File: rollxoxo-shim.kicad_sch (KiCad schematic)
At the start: 1 part, among them J1 Conn_01x10

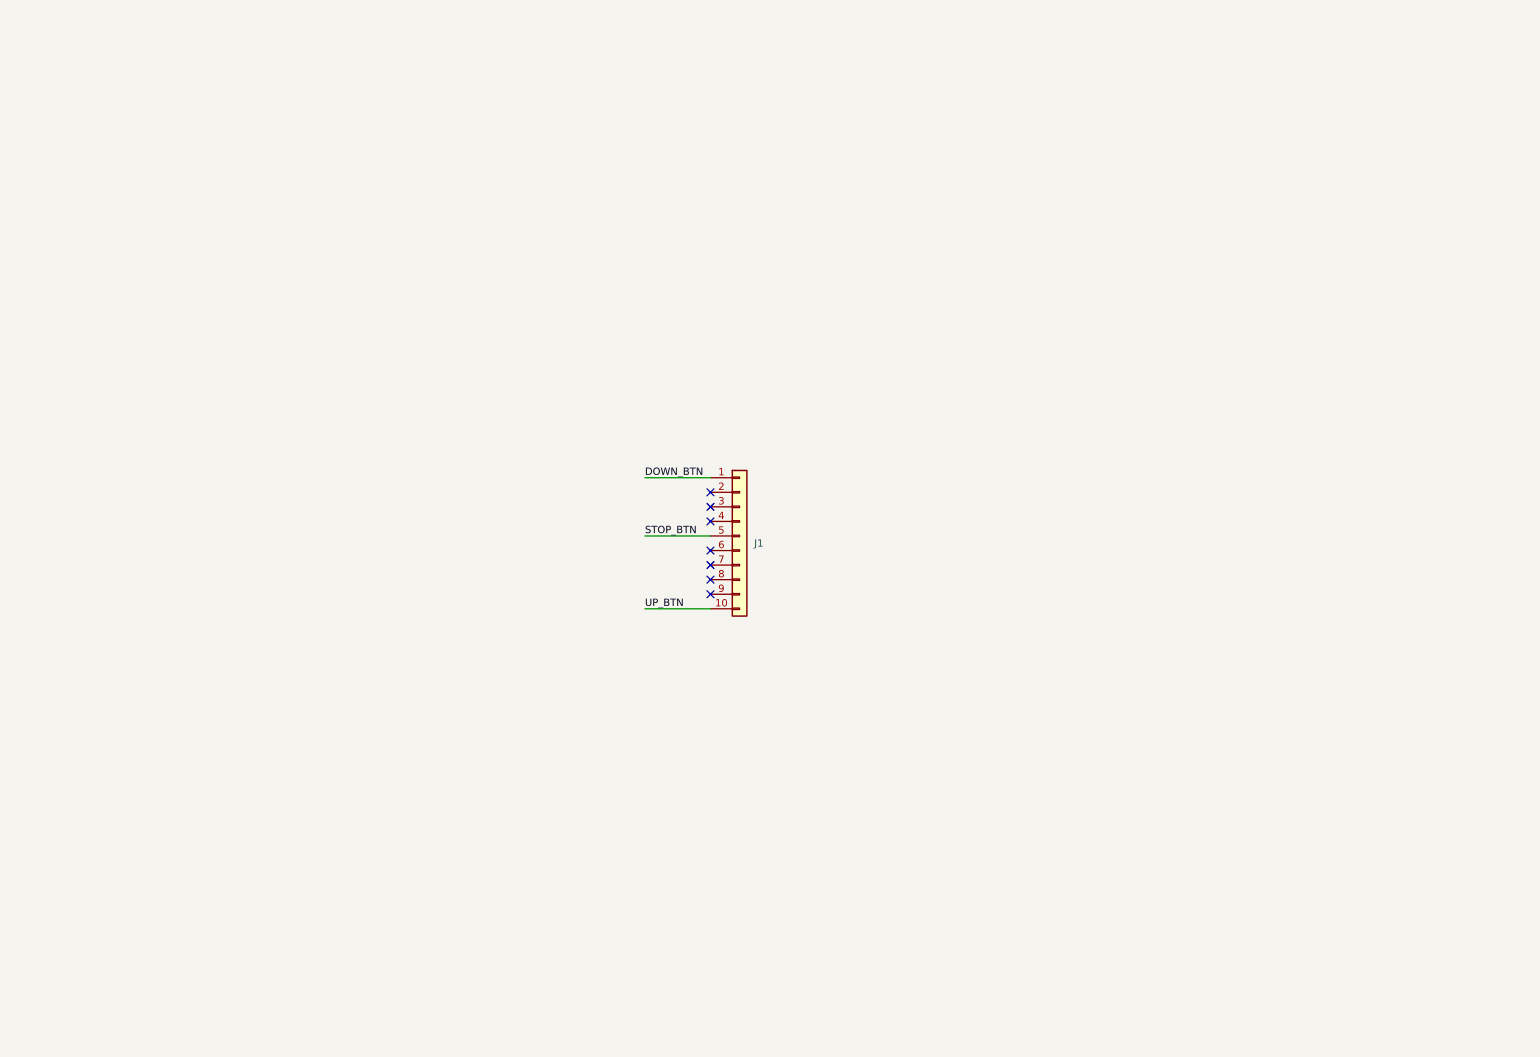
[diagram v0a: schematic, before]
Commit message: schem: import esp32 and support circuits
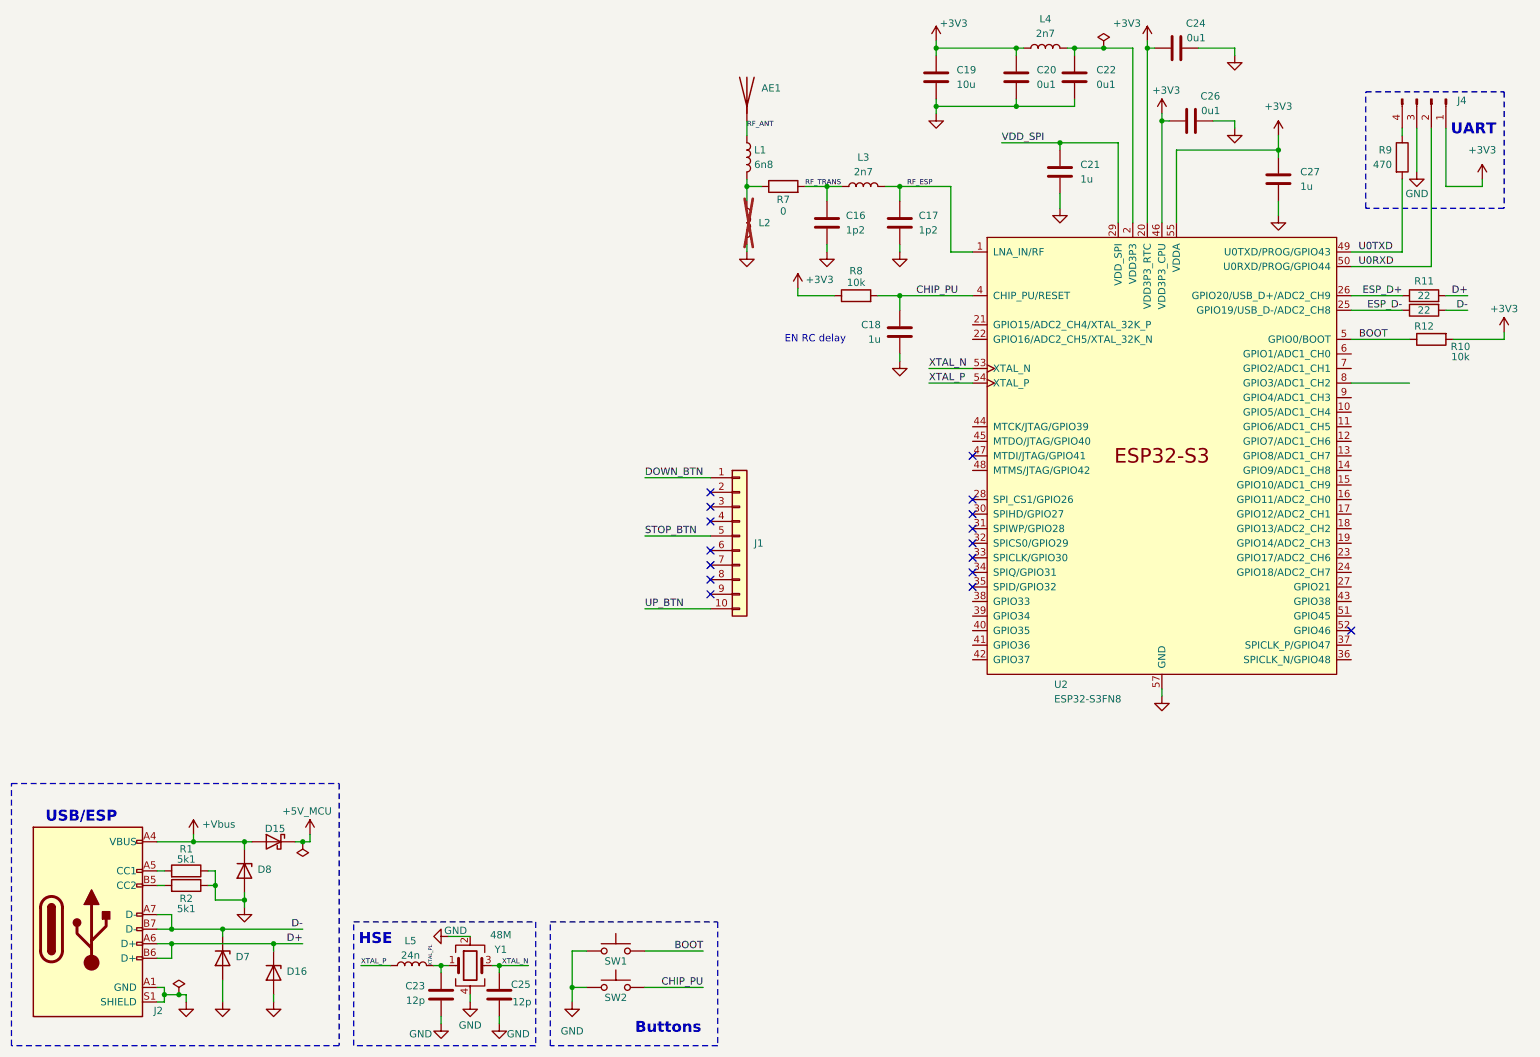
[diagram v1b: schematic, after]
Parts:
- added AE1: Antenna, RF_Antenna:Johanson_2450AT18x100, symbol Device:Antenna
- added C16, C17: 1p2, Capacitor_SMD:C_0402_1005Metric, symbol Device:C
- added C18, C21, C27: 1u, Capacitor_SMD:C_0402_1005Metric, symbol Device:C
- added C19: 10u, Capacitor_SMD:C_0402_1005Metric, symbol Device:C
- added C20, C22, C24, C26: 0u1, Capacitor_SMD:C_0402_1005Metric, symbol Device:C
- added C23, C25: 12p, Capacitor_SMD:C_0402_1005Metric, symbol Device:C
- added D15: D_Schottky, Diode_SMD:D_SMA, symbol Device:D_Schottky
- added D16, D7, D8: H5VU10U, GLCS:Diode_DFN1006, symbol GLCS:H5VU10U
- added J2: USB_C_Receptacle_USB2.0_14P, Connector_USB:USB_C_Receptacle_HRO_TYPE-C-31-M-12, symbol Connector:USB_C_Receptacle_USB2.0_14P
- added J4: Conn_01x04_Pin, Connector_PinHeader_2.54mm:PinHeader_1x04_P2.54mm_Vertical, symbol Connector:Conn_01x04_Pin
- added L1: 6n8, Inductor_SMD:L_0402_1005Metric, symbol Device:L
- added L2: L, Inductor_SMD:L_0402_1005Metric, symbol Device:L
- added L3, L4: 2n7, Inductor_SMD:L_0402_1005Metric, symbol Device:L
- added L5: 24n, Inductor_SMD:L_0402_1005Metric, symbol Device:L
- added R1, R2: 5k1, Resistor_SMD:R_0402_1005Metric, symbol Device:R
- added R10, R8: 10k, Resistor_SMD:R_0402_1005Metric, symbol Device:R
- added R11, R12: 22, Resistor_SMD:R_0402_1005Metric, symbol Device:R
- added R7: 0, Resistor_SMD:R_0402_1005Metric, symbol Device:R
- added R9: 470, Resistor_SMD:R_0402_1005Metric, symbol Device:R
- added SW1, SW2: SW_Push, Button_Switch_SMD:SW_SPST_TS-1088-xR020, symbol Switch:SW_Push
- added U2: ESP32-S3FN8, Package_DFN_QFN:QFN-56-1EP_7x7mm_P0.4mm_EP4x4mm_ThermalVias, symbol PCM_Espressif:ESP32-S3
- added Y1: 48M, Crystal:Crystal_SMD_2016-4Pin_2.0x1.6mm, symbol Device:Crystal_GND24
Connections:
- new net: J2.B5 (CC2), R2.2
- new net: L1.2, L2.1, R7.1
- new net: J4.4 (Pin_4), R9.1
- new net: J2.A5 (CC1), R1.2
- new net +3V3: C19.1, C20.1, C24.1, C26.1, C27.1, J4.1 (Pin_1), L4.1, R10.2, R8.1, U2.20 (VDD3P3_RTC), U2.46 (VDD3P3_CPU), U2.55 (VDDA), U2.56 (VDDA)
- new net +5V_MCU: D15.1 (K)
- new net +Vbus: D15.2 (A), D8.1 (K), J2.A4 (VBUS), J2.A9 (VBUS), J2.B4 (VBUS), J2.B9 (VBUS)
- new net BOOT: R10.1, SW1.2, U2.5 (GPIO0/BOOT)
- new net CHIP_PU: C18.1, R8.2, SW2.2, U2.4 (CHIP_PU/RESET)
- new net D+: D16.1 (K), J2.A6 (D+), J2.B6 (D+), R11.2
- new net D-: D7.1 (K), J2.A7 (D-), J2.B7 (D-), R12.2
- new net ESP_D+: R11.1, U2.26 (GPIO20/USB_D+/ADC2_CH9)
- new net ESP_D-: R12.1, U2.25 (GPIO19/USB_D-/ADC2_CH8)
- new net GND: C16.2, C17.2, C18.2, C19.2, C20.2, C21.2, C22.2, C23.1, C24.2, C25.2, C26.2, C27.2, D16.2 (A), D7.2 (A), D8.2 (A), J2.A1 (GND), J2.A12 (GND), J2.B1 (GND), J2.B12 (GND), J2.S1 (SHIELD), J4.3 (Pin_3), L2.2, R1.1, R2.1, SW1.1, SW2.1, U2.57 (GND), Y1.2, Y1.4
- new net RF_ANT: AE1.1 (A), L1.1
- new net RF_ESP: C17.1, L3.2, U2.1 (LNA_IN/RF)
- new net RF_TRANS: C16.1, L3.1, R7.2
- new net U0RXD: J4.2 (Pin_2), U2.50 (U0RXD/PROG/GPIO44)
- new net U0TXD: R9.2, U2.49 (U0TXD/PROG/GPIO43)
- new net VDD3P3: C22.1, L4.2, U2.2 (VDD3P3), U2.3 (VDD3P3)
- new net VDD_SPI: C21.1, U2.29 (VDD_SPI)
- new net XTAL_N: C25.1, U2.53 (XTAL_N), Y1.3
- new net XTAL_P: L5.1, U2.54 (XTAL_P)
- new net XTAL_PL: C23.2, L5.2, Y1.1
- no-connect marks 7 -> 16
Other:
- note added: "Buttons"
- note added: "EN RC delay"
- note added: "HSE"
- note added: "UART"
- note added: "USB/ESP"

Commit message: schem: add SN74LV1T125DBV level shifters
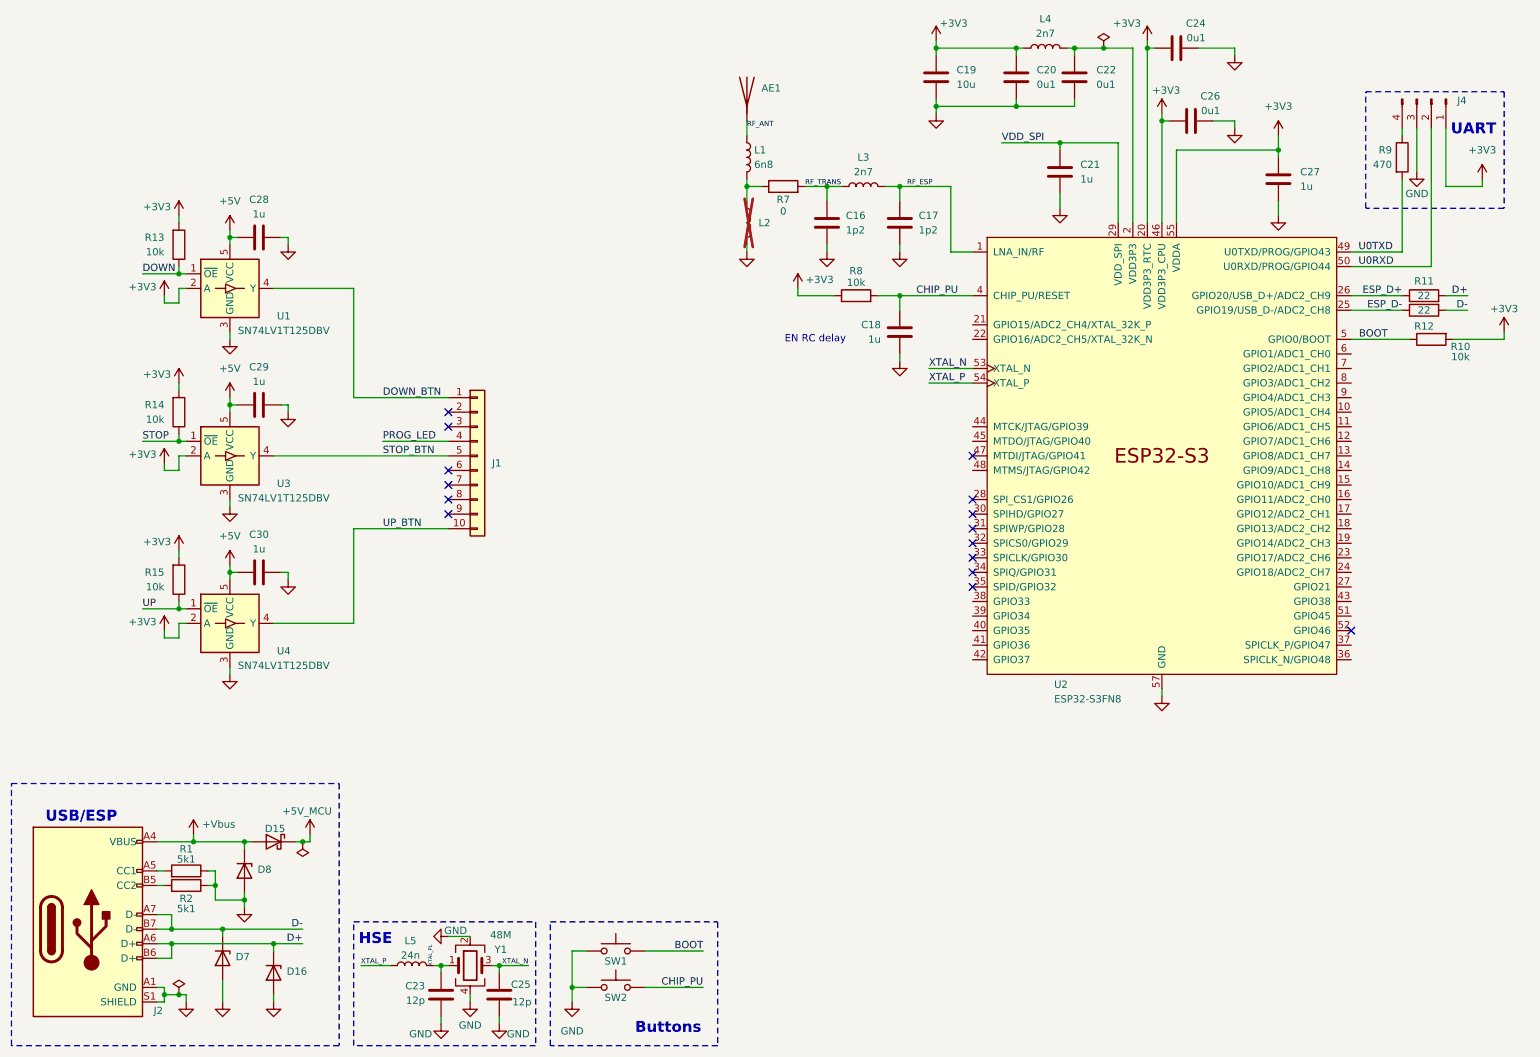
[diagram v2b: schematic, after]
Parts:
- added C28, C29, C30: 1u, Capacitor_SMD:C_0402_1005Metric, symbol Device:C
- added R13, R14, R15: 10k, Resistor_SMD:R_0402_1005Metric, symbol Device:R
- added U1, U3, U4: SN74LV1T125DBV, Package_TO_SOT_SMD:SOT-23-5, symbol Logic_LevelTranslator:SN74LV1T125DBV
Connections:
- net +3V3: now also R13.2, R14.2, R15.2, U1.2 (A), U3.2 (A), U4.2 (A)
- net DOWN_BTN: now also U1.4 (Y)
- net GND: now also C28.2, C29.2, C30.2, U1.3 (GND), U3.3 (GND), U4.3 (GND)
- net STOP_BTN: now also U3.4 (Y)
- net UP_BTN: now also U4.4 (Y)
- net PROG_LED: now reaches J1.4 (Pin_4)
- new net +5V: C28.1, C29.1, C30.1, U1.5 (VCC), U3.5 (VCC), U4.5 (VCC)
- new net DOWN: R13.1, U1.1 (~{OE})
- new net STOP: R14.1, U3.1 (~{OE})
- new net UP: R15.1, U4.1 (~{OE})
- no-connect marks 16 -> 15
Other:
- moved on the sheet: J1

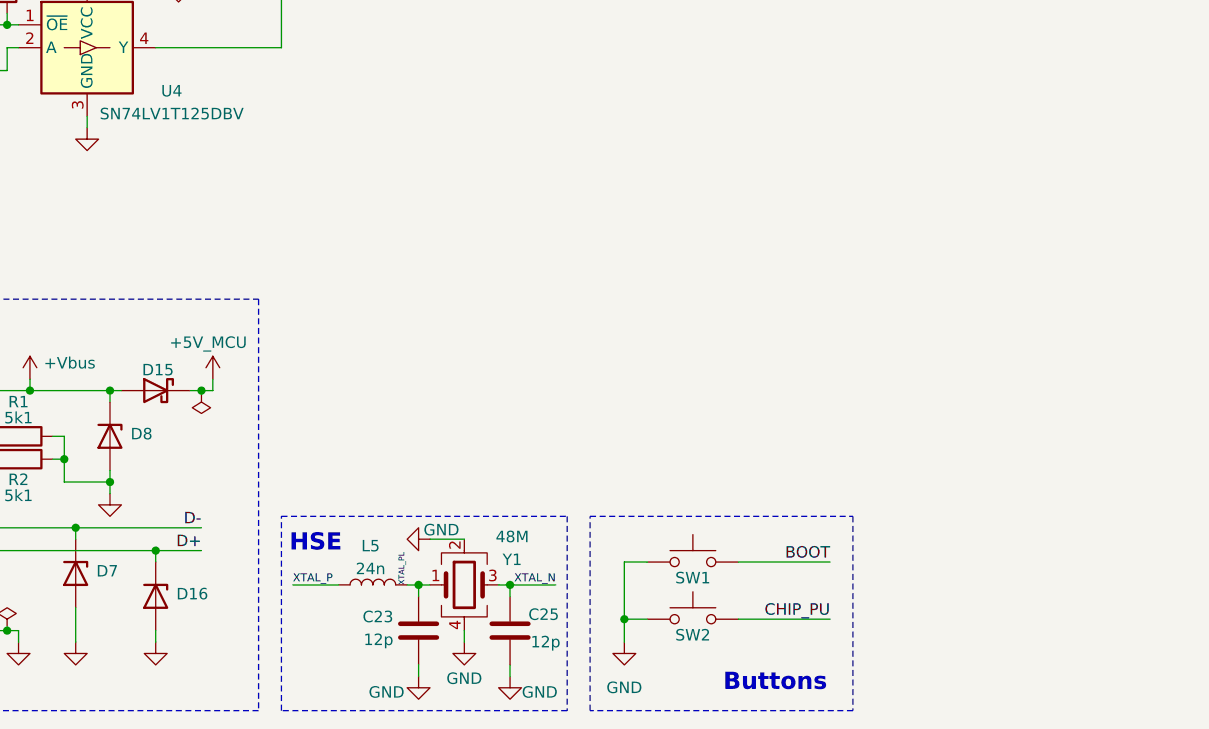
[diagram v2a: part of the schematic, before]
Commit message: schem: add TPSM84338 24V power module
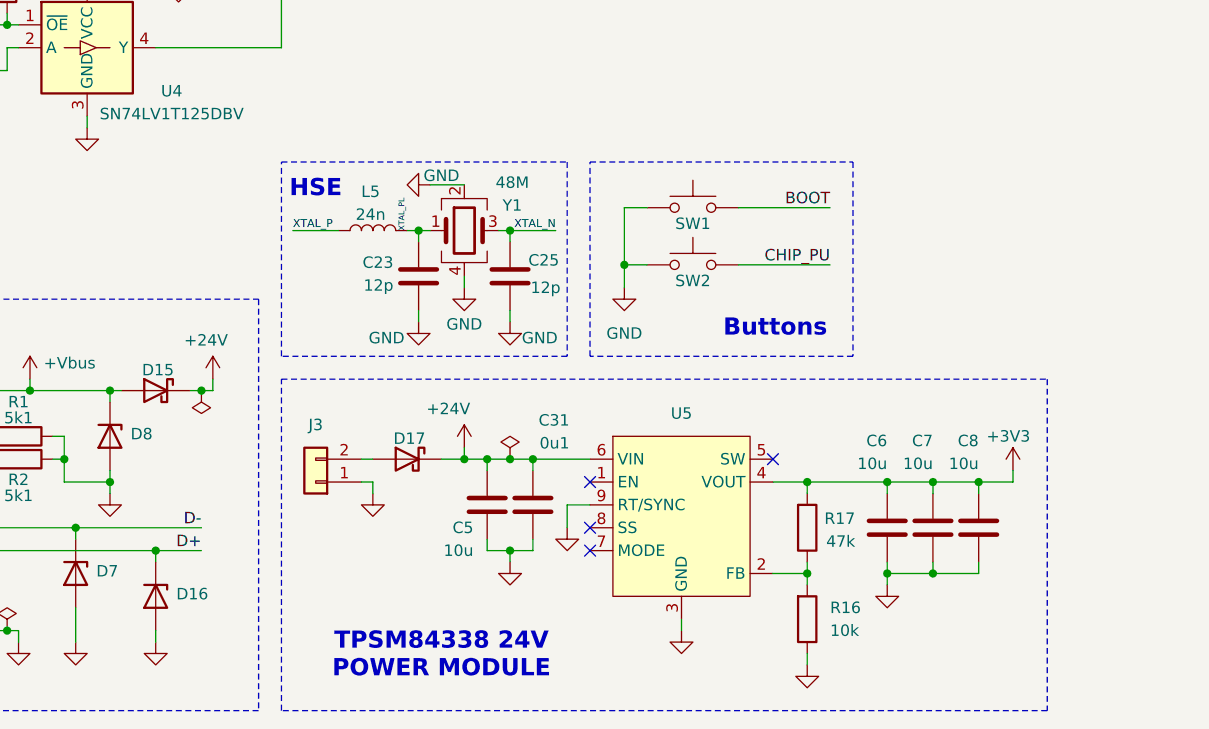
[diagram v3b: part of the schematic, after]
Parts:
- added C31: 0u1, Capacitor_SMD:C_0402_1005Metric, symbol Device:C
- added C5, C6, C7, C8: 10u, Capacitor_SMD:C_0805_2012Metric, symbol Device:C
- added D17: D_Schottky, Diode_SMD:D_SMA, symbol Device:D_Schottky
- added J3: Conn_01x02, Connector_JST:JST_XH_S2B-XH-A_1x02_P2.50mm_Horizontal, symbol Connector_Generic:Conn_01x02
- added R16: 10k, Resistor_SMD:R_0402_1005Metric, symbol Device:R
- added R17: 47k, Resistor_SMD:R_0402_1005Metric, symbol Device:R
- added U5: (no value), GLCS:TPSM84338, symbol GLCS:TPSM84338
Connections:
- net +3V3: now also C6.1, C7.1, C8.1, R17.2, U5.4 (VOUT)
- net GND: now also C31.2, C5.2, C6.2, C7.2, C8.2, J3.1 (Pin_1), R16.1, U5.3 (GND), U5.9 (RT/SYNC)
- net +5V_MCU renamed +24V
- net +24V: now also C31.1, C5.1, D17.1 (K), U5.6 (VIN)
- new net: R16.2, R17.1, U5.2 (FB)
- new net: D17.2 (A), J3.2 (Pin_2)
- no-connect marks 15 -> 19
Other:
- note added: "TPSM84338 24V POWER MODULE"
- moved on the sheet: C23, C25, L5, SW1, SW2, Y1
